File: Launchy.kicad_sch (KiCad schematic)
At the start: 38 parts, among them IC1 ESP32-C3-MINI-1-N4, IC2 SBC846BPDW1T3G, J1 Conn_02x06_Odd_Even, J2 Conn_01x02, J3 Conn_01x01_Socket, J4 Conn_01x01_Socket, J5 Screw_Terminal_01x03, J6 USB_C_Receptacle_USB2.0_16P, K1 SRD-03VDC-SL-C, Q1 IRLML0030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

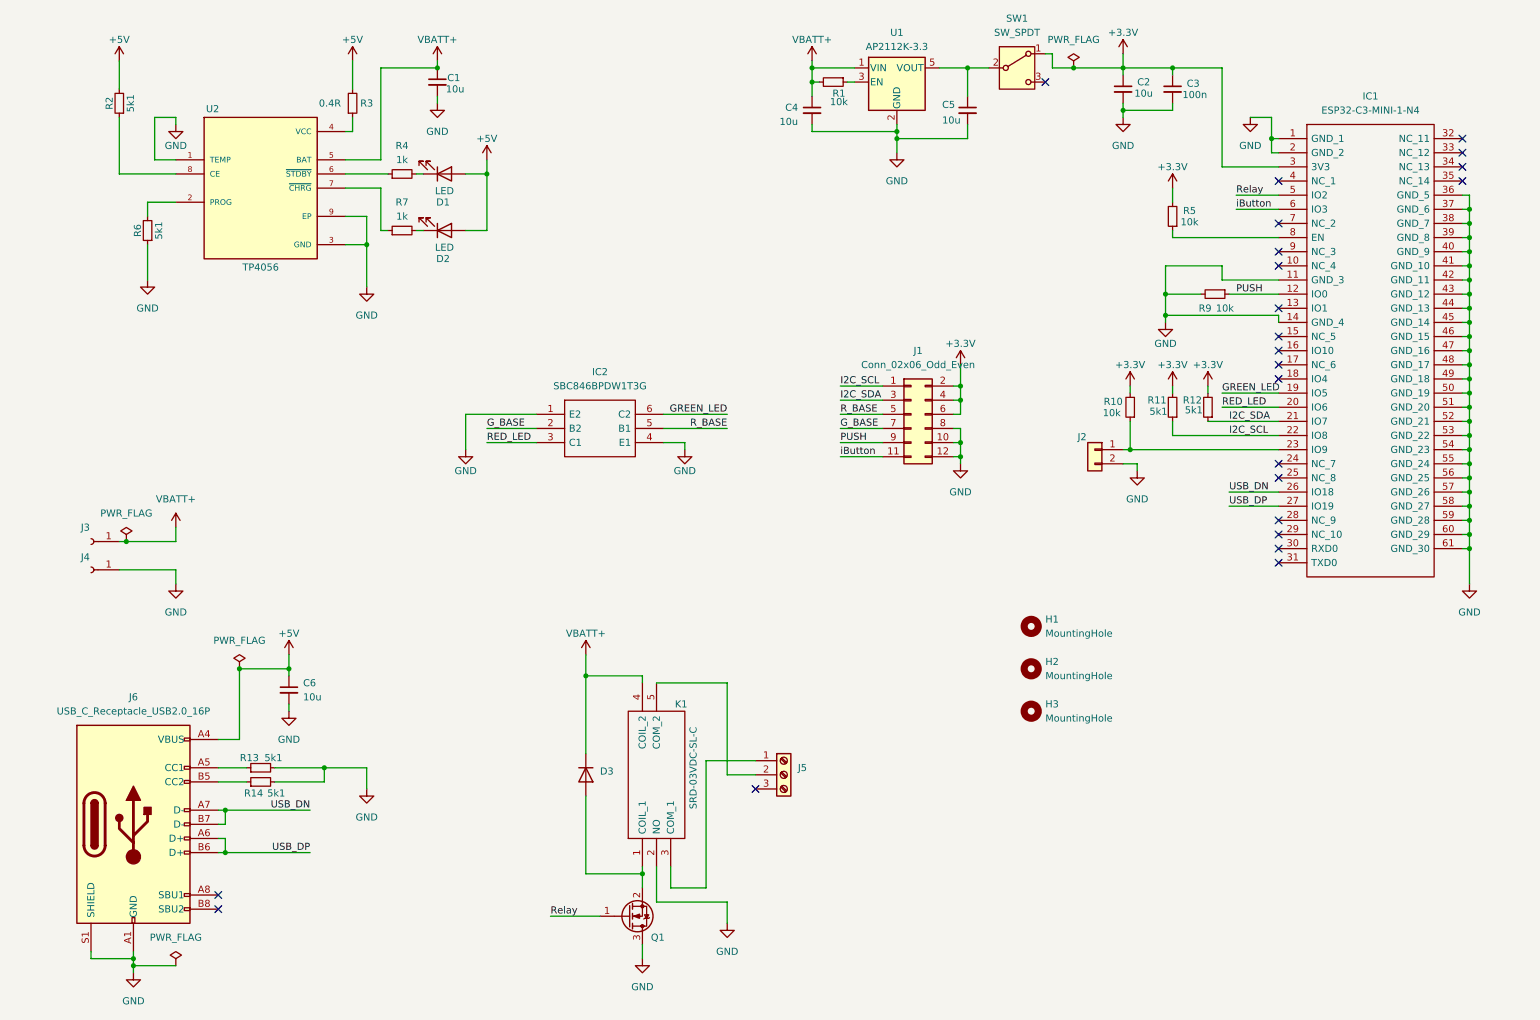
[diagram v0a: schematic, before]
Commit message: Quality of life changes in Code Symbol and footprint libraries include Schematic and pcb updates, unnecessary dual bjt remove, replacing 2.00mm headers with more common 2.54mm ones Copper Pour tweaks Adding Display demo
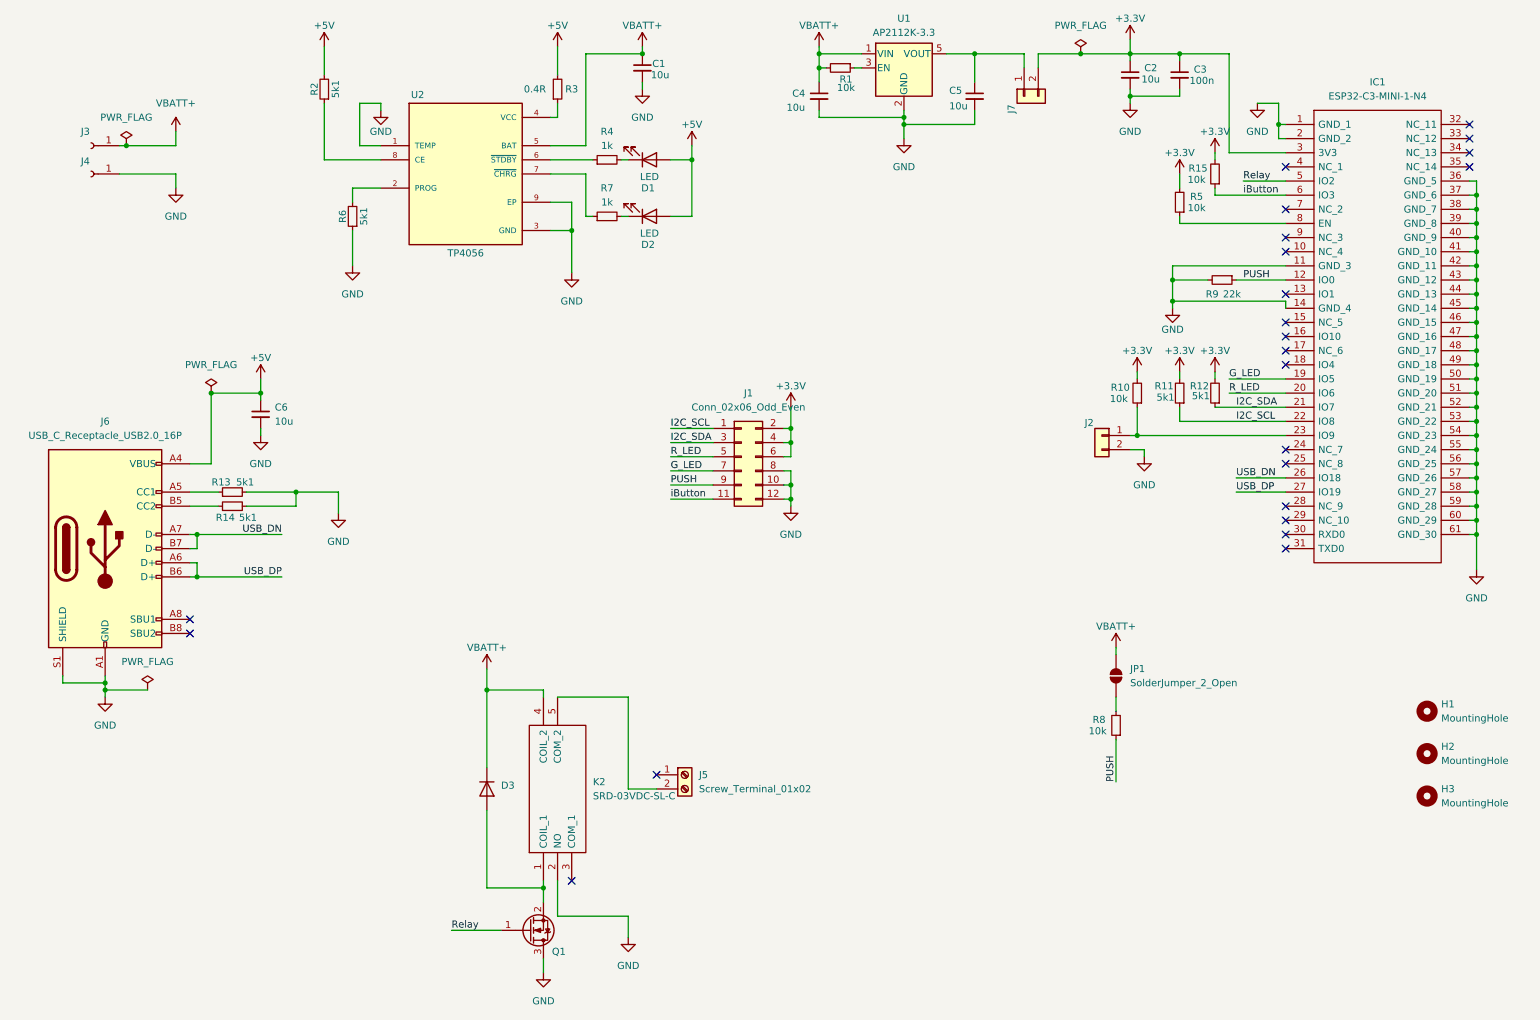
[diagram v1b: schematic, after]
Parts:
- removed IC2: SBC846BPDW1T3G, SamacSys_Parts:SOT65P210X110-6N, symbol SamacSys_Parts:SBC846BPDW1T3G
- removed J5: Screw_Terminal_01x03, Connector_PinSocket_2.54mm:PinSocket_1x03_P2.54mm_Vertical, symbol Connector:Screw_Terminal_01x03
- removed K1: SRD-03VDC-SL-C, SamacSys_Parts:SRD03VDCSLC, symbol SamacSys_Parts:SRD-03VDC-SL-C
- removed SW1: SW_SPDT, Connector_PinHeader_2.00mm:PinHeader_1x03_P2.00mm_Vertical, symbol Switch:SW_SPDT
- added J5: Screw_Terminal_01x02, TerminalBlock:TerminalBlock_MaiXu_MX126-5.0-02P_1x02_P5.00mm, symbol Library:Screw_Terminal_01x02
- added J7: Conn_01x02, Connector_PinHeader_2.54mm:PinHeader_1x02_P2.54mm_Vertical, symbol Library:Conn_01x02
- added JP1: SolderJumper_2_Open, Jumper:SolderJumper-2_P1.3mm_Open_TrianglePad1.0x1.5mm, symbol Library:SolderJumper_2_Open
- added K2: SRD-03VDC-SL-C, SamacSys_Parts:SRD03VDCSLC, symbol Library:SRD-03VDC-SL-C
- added R15, R8: 10k, Capacitor_SMD:C_1206_3216Metric_Pad1.33x1.80mm_HandSolder, symbol Library:R_Small
- C1, C2, C3, C4, C5, C6: symbol Device:C_Small -> Library:C_Small
- D1, D2: symbol Device:LED -> Library:LED
- D3: symbol Diode:1N5404 -> Library:1N5404
- H1, H2, H3: symbol Mechanical:MountingHole -> Library:MountingHole
- IC1: symbol SamacSys_Parts:ESP32-C3-MINI-1-N4 -> Library:ESP32-C3-MINI-1-N4
- J1: footprint Connector_PinHeader_2.00mm:PinHeader_2x06_P2.00mm_Vertical -> Connector_PinHeader_2.54mm:PinHeader_2x06_P2.54mm_Vertical; symbol Connector_Generic:Conn_02x06_Odd_Even -> Library:Conn_02x06_Odd_Even
- J2: symbol Connector_Generic:Conn_01x02 -> Library:Conn_01x02
- J3: symbol Connector:Conn_01x01_Socket -> Library:Conn_01x01_Socket_1
- J4: symbol Connector:Conn_01x01_Socket -> Library:Conn_01x01_Socket
- J6: symbol Connector:USB_C_Receptacle_USB2.0_16P -> Library:USB_C_Receptacle_USB2.0_16P
- Q1: symbol Transistor_FET:IRLML0030 -> Library:IRLML0030
- R1, R10, R11, R12, R13, R14, R2, R3, R4, R5, R6, R7: symbol Device:R_Small -> Library:R_Small
- R9: value 10k -> 22k; symbol Device:R_Small -> Library:R_Small
- U1: symbol Regulator_Linear:AP2112K-3.3 -> Library:AP2112K-3.3
- U2: symbol Customsymbols:TP4056 -> Library:TP4056
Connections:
- net G_BASE is gone; now on net G_LED: J1.7 (Pin_7)
- net R_BASE is gone; now on net R_LED: J1.5 (Pin_5)
- net +3.3V: now also J7.2 (Pin_2), R15.2
- net GND: now also K2.2 (NO)
- net PUSH: now also R8.1
- net VBATT+: now also JP1.1 (A), K2.4 (COIL_2)
- net iButton: now also R15.1
- net at C5.1, U1.5 (VOUT): now also J7.1 (Pin_1)
- net at D3.2 (A), Q1.2 (S): now also K2.1 (COIL_1)
- net GREEN_LED renamed G_LED
- net RED_LED renamed R_LED
- new net: J5.2 (Pin_2), K2.5 (COM_2)
- new net: JP1.2 (B), R8.2
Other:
- moved on the sheet: C1, C2, C3, C4, C5, C6, D1, D2, D3, H1, H2, H3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
